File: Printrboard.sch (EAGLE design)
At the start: 127 parts, among them J1 MICROSD, J3 USB-MICRO-PTH, J4 PCIE, Q1 RFP30N06LE, Q2 RFP30N06LE, Q3 RFP30N06LE, U1 LM2841, U10 MCP4728, U2 A4982, U3 A4982, U4 A4982, U5 A4982, U6 AT90USB1286, U7 AP7313, U8 TXB0104, U9 PRTR5V0U4D, X1 16MHz

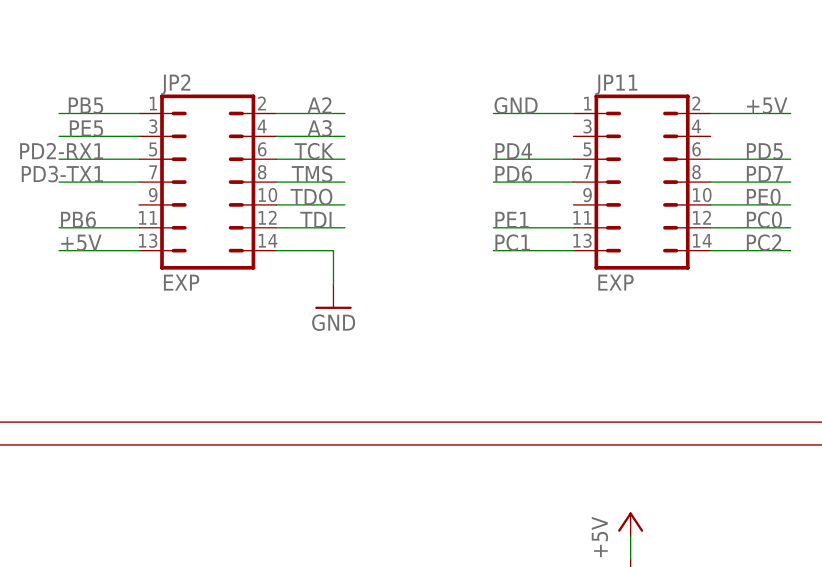
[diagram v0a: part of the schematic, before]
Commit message: Manufacturability changes
Added some pin 1 indicators
Added test point for VBUS signal
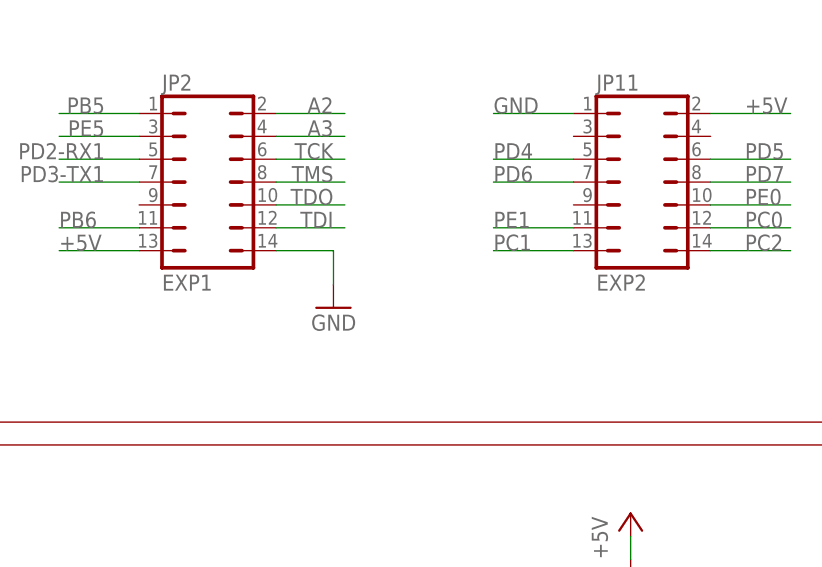
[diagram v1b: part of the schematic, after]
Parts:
- JP11: value EXP -> EXP2
- JP2: value EXP -> EXP1
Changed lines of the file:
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@@
 <part name="JP8" library="SparkFun" deviceset="M03" device="POLAR" value="Y-STOP"/>
 <part name="JP10" library="SparkFun" deviceset="M03" device="POLAR" value="Z-STOP"/>
-<part name="JP2" library="printrbot" deviceset="JP7Q" device="" value="EXP"/>
-<part name="JP11" library="printrbot" deviceset="JP7Q" device="" value="EXP"/>
+<part name="JP2" library="printrbot" deviceset="JP7Q" device="" value="EXP1"/>
+<part name="JP11" library="printrbot" deviceset="JP7Q" device="" value="EXP2"/>
 <part name="JP4" library="printrbot" deviceset="JP3Q" device="" value="ICSP"/>
 <part name="C34" library="ipc-7351-capacitor" deviceset="CAPACITOR_" device="0805" value="0.1uF"/>

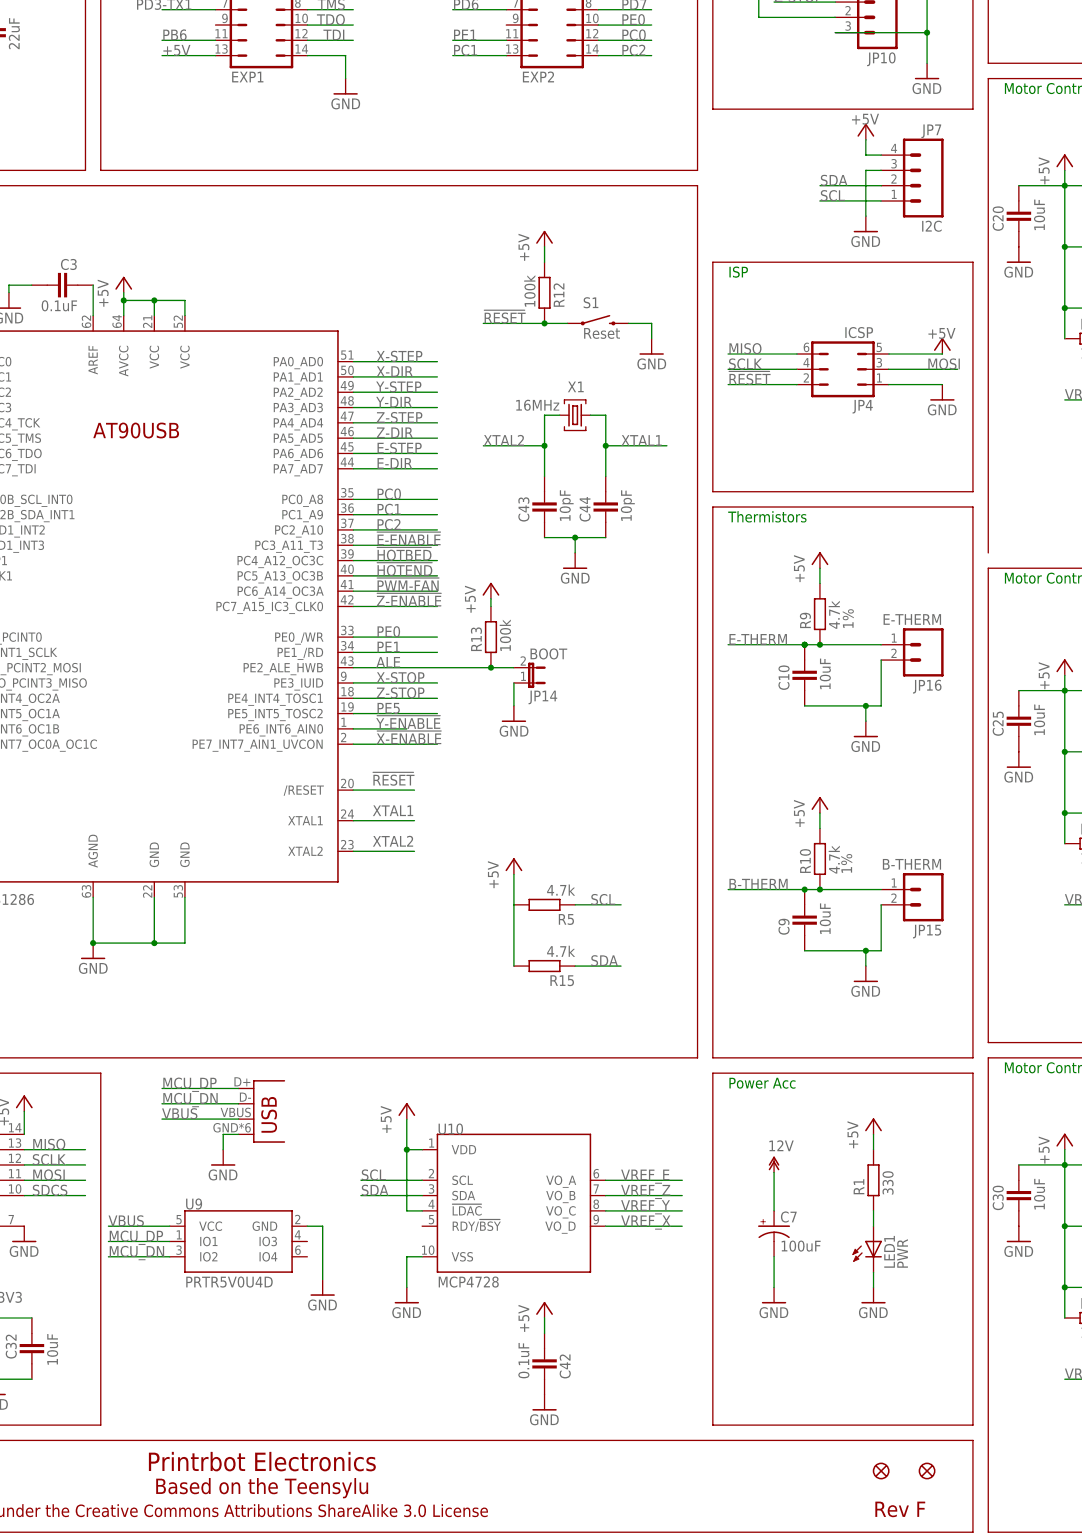
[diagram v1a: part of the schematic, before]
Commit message: Minor schematic changes
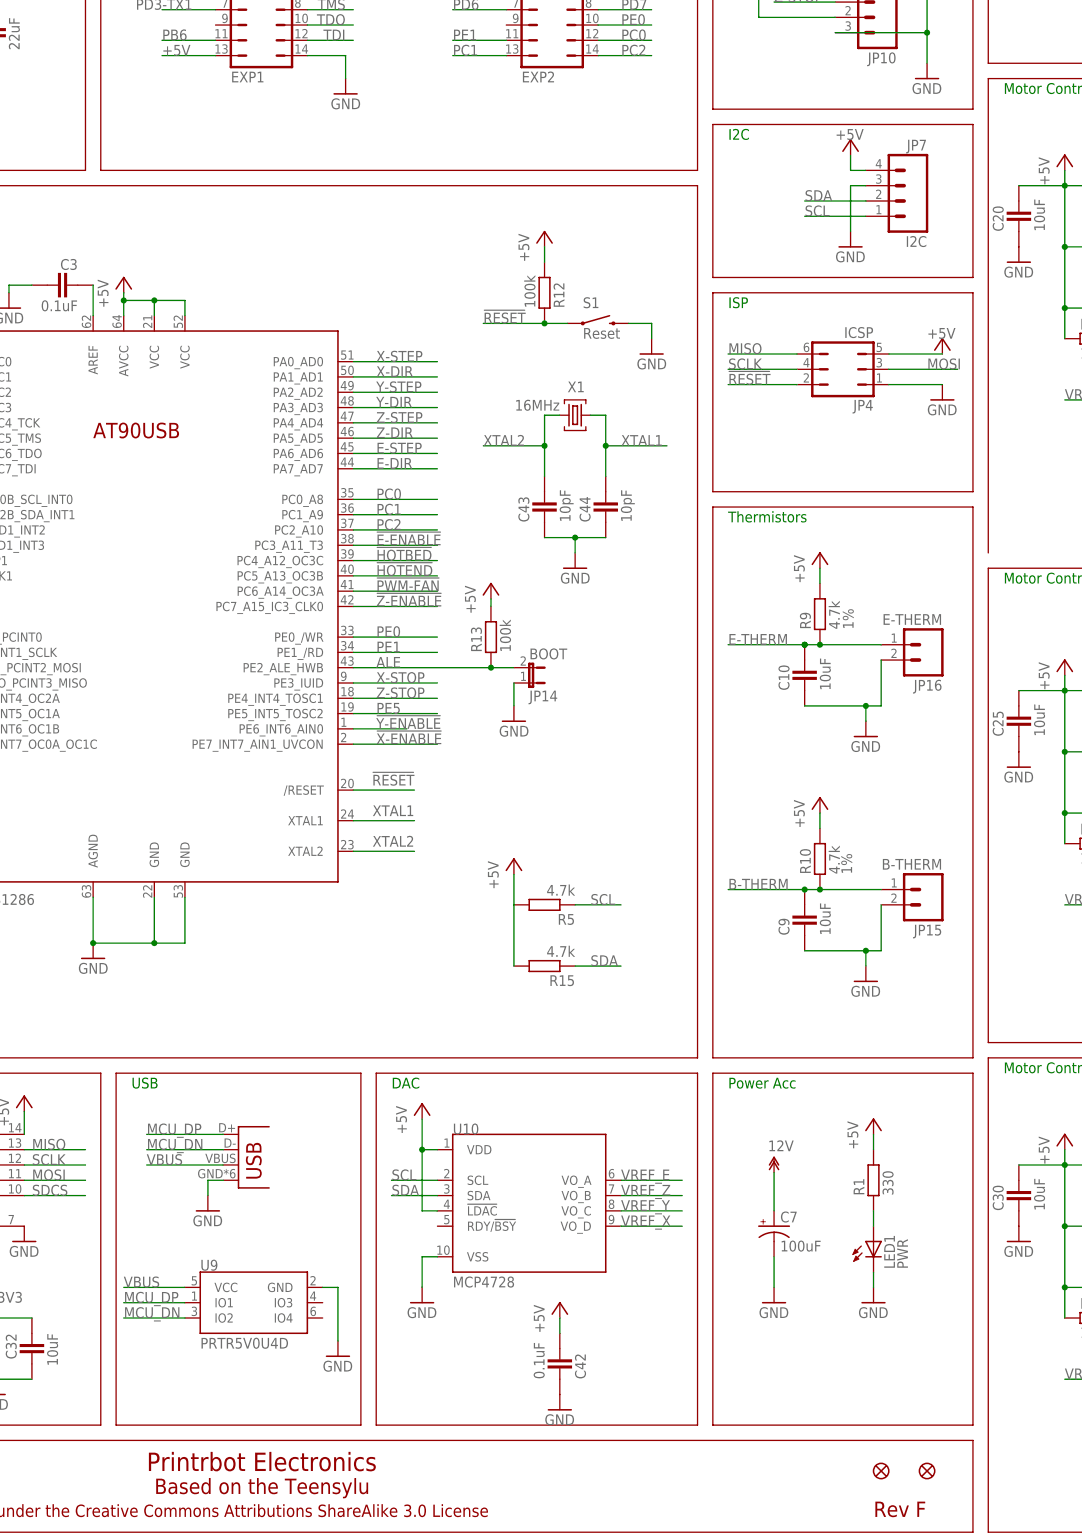
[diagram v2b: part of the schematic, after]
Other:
- note added: "DAC"
- note added: "I2C"
- note added: "USB"
- moved on the sheet: C42, JP7, U10, U9

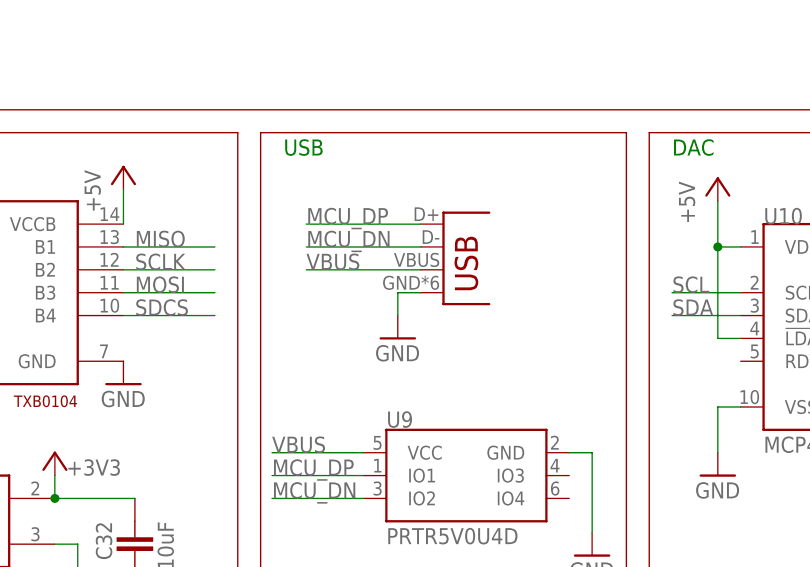
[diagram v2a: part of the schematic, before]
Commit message: Redraw USB connector for manufacturability
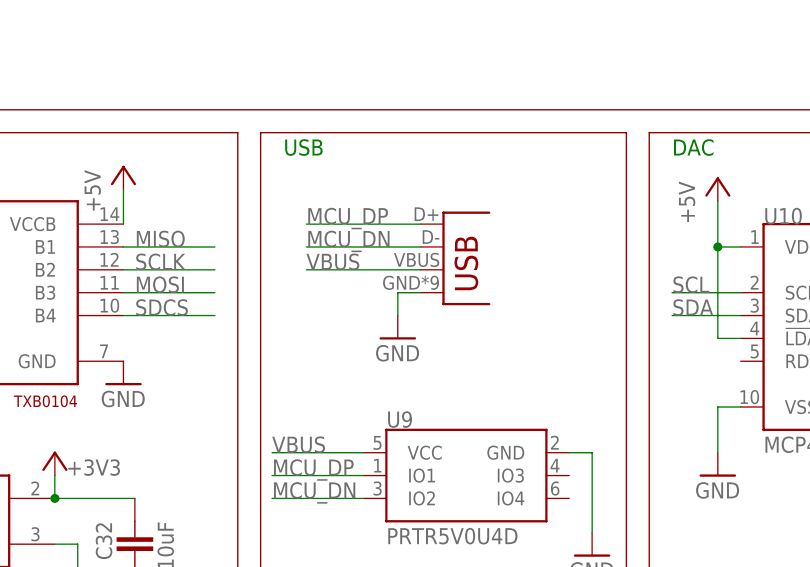
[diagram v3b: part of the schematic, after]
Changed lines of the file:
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@@
 <?xml version="1.0" encoding="utf-8"?>
 <!DOCTYPE eagle SYSTEM "eagle.dtd">
-<eagle version="6.1">
+<eagle version="6.6.0">
 <drawing>
 <settings>

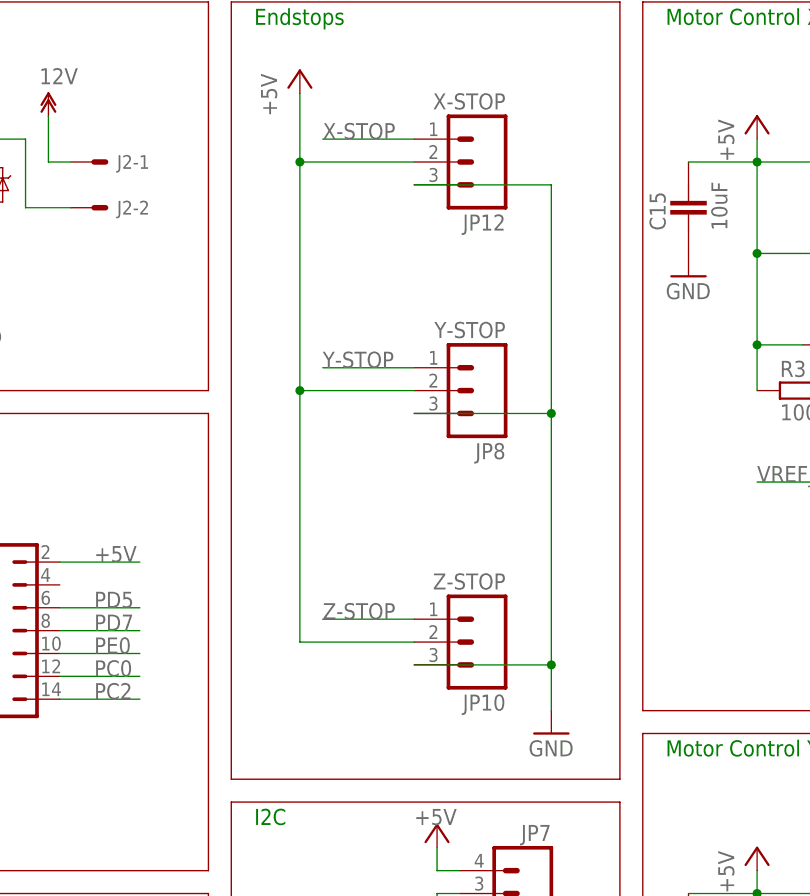
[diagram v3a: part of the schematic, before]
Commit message: Add in voltage selection and input buffering for the Z-stop
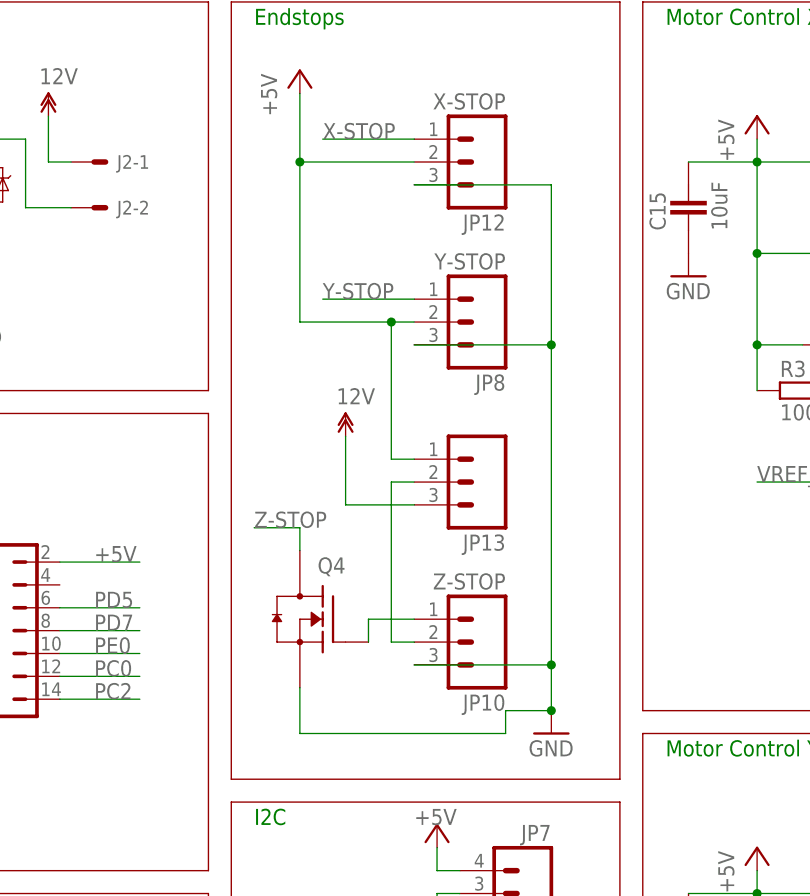
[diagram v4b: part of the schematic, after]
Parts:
- added JP13: (no value), SparkFun:M03PTH
- added Q4: RFP30N06LE, ipc-7351-transistor:MOSFET-NCH_SOT-23
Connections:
- new net N$6: JP10.1, Q4.G
- new net N$8: JP10.2, JP13.2
- net +5V: now also JP13.1; no longer JP10.2
- net 12V: now also JP13.3
- net GND: now also Q4.S
- net Z-STOP: now also Q4.D; no longer JP10.1
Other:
- moved on the sheet: JP8
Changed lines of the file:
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@@
 <part name="GND52" library="SparkFun" deviceset="GND" device=""/>
 <part name="D2" library="printrbot" deviceset="SCH-DIODE" device="SMA" value=""/>
+<part name="Q4" library="ipc-7351-transistor" deviceset="MOSFET-NCH_" device="SOT-23" value="RFP30N06LE"/>
+<part name="U$6" library="12v" deviceset="12V" device=""/>
+<part name="JP13" library="SparkFun" deviceset="M03" device="PTH"/>
 </parts>
 <sheets>
@@
 </instance>
 <instance part="JP6" gate="G$1" x="127" y="220.98" rot="MR0"/>
-<instance part="JP8" gate="G$1" x="223.52" y="198.12" rot="R180"/>
+<instance part="JP8" gate="G$1" x="223.52" y="205.74" rot="R180"/>
 <instance part="JP10" gate="G$1" x="223.52" y="170.18" rot="R180"/>
 <instance part="JP2" gate="B" x="120.65" y="171.45" rot="R270"/>
@@
 <instance part="GND52" gate="1" x="172.72" y="78.74" rot="MR0"/>
 <instance part="D2" gate="G$1" x="60.96" y="215.9" rot="R90"/>
+<instance part="Q4" gate="G$1" x="208.28" y="172.72" smashed="yes" rot="MR0">
+<attribute name="NAME" x="208.28" y="177.8" size="1.778" layer="95" rot="MR0"/>
+</instance>
+<instance part="U$6" gate="G$1" x="208.28" y="193.04"/>
+<instance part="JP13" gate="G$1" x="223.52" y="187.96" rot="R180"/>
 </instances>
 <busses>
@@
 <segment>
 <wire x1="215.9" y1="220.98" x2="231.14" y2="220.98" width="0.1524" layer="91"/>
-<wire x1="231.14" y1="220.98" x2="231.14" y2="195.58" width="0.1524" layer="91"/>
-<wire x1="231.14" y1="195.58" x2="231.14" y2="167.64" width="0.1524" layer="91"/>
+<wire x1="231.14" y1="220.98" x2="231.14" y2="203.2" width="0.1524" layer="91"/>
+<wire x1="231.14" y1="203.2" x2="231.14" y2="167.64" width="0.1524" layer="91"/>
 <wire x1="231.14" y1="167.64" x2="231.14" y2="162.56" width="0.1524" layer="91"/>
-<wire x1="215.9" y1="195.58" x2="231.14" y2="195.58" width="0.1524" layer="91"/>
+<wire x1="215.9" y1="203.2" x2="231.14" y2="203.2" width="0.1524" layer="91"/>
 <wire x1="215.9" y1="167.64" x2="231.14" y2="167.64" width="0.1524" layer="91"/>
-<junction x="231.14" y="195.58"/>
+<junction x="231.14" y="203.2"/>
 <junction x="231.14" y="167.64"/>
 <pinref part="JP12" gate="G$1" pin="3"/>
@@
 <pinref part="JP8" gate="G$1" pin="3"/>
 <pinref part="JP10" gate="G$1" pin="3"/>
+<wire x1="203.2" y1="160.02" x2="226.06" y2="160.02" width="0.1524" layer="91"/>
+<wire x1="226.06" y1="160.02" x2="226.06" y2="162.56" width="0.1524" layer="91"/>
+<wire x1="226.06" y1="162.56" x2="231.14" y2="162.56" width="0.1524" layer="91"/>
+<junction x="231.14" y="162.56"/>
+<pinref part="Q4" gate="G$1" pin="S"/>
+<wire x1="203.2" y1="160.02" x2="203.2" y2="165.1" width="0.1524" layer="91"/>
 </segment>
 <segment>
@@
 <junction x="5.08" y="220.98"/>
 </segment>
+<segment>
+<pinref part="JP13" gate="G$1" pin="3"/>
+<wire x1="215.9" y1="185.42" x2="208.28" y2="185.42" width="0.1524" layer="91"/>
+<wire x1="208.28" y1="185.42" x2="208.28" y2="193.04" width="0.1524" layer="91"/>
+<pinref part="U$6" gate="G$1" pin="12V"/>
+</segment>
 </net>
 <net name="MISO" class="0">
@@
 <net name="Y-STOP" class="0">
 <segment>
-<wire x1="215.9" y1="200.66" x2="205.74" y2="200.66" width="0.1524" layer="91"/>
-<label x="205.74" y="200.66" size="1.778" layer="95"/>
+<wire x1="215.9" y1="208.28" x2="205.74" y2="208.28" width="0.1524" layer="91"/>
+<label x="205.74" y="208.28" size="1.778" layer="95"/>
 <pinref part="JP8" gate="G$1" pin="1"/>
 </segment>
@@
 <net name="Z-STOP" class="0">
 <segment>
-<wire x1="215.9" y1="172.72" x2="205.74" y2="172.72" width="0.1524" layer="91"/>
-<label x="205.74" y="172.72" size="1.778" layer="95"/>
-<pinref part="JP10" gate="G$1" pin="1"/>
-</segment>
-<segment>
 <wire x1="135.89" y1="57.15" x2="149.86" y2="57.15" width="0.1524" layer="91"/>
 <label x="139.7" y="57.15" size="1.778" layer="95"/>
 <pinref part="U6" gate="G$1" pin="PE4_INT4_TOSC1"/>
+</segment>
+<segment>
+<wire x1="203.2" y1="182.88" x2="198.12" y2="182.88" width="0.1524" layer="91"/>
+<label x="198.12" y="182.88" size="1.778" layer="95"/>
+<pinref part="Q4" gate="G$1" pin="D"/>
+<wire x1="203.2" y1="180.34" x2="203.2" y2="182.88" width="0.1524" layer="91"/>
 </segment>
 </net>
@@
 </segment>
 <segment>
-<wire x1="215.9" y1="170.18" x2="203.2" y2="170.18" width="0.1524" layer="91"/>
-<wire x1="215.9" y1="198.12" x2="203.2" y2="198.12" width="0.1524" layer="91"/>
+<wire x1="215.9" y1="205.74" x2="213.36" y2="205.74" width="0.1524" layer="91"/>
+<wire x1="213.36" y1="205.74" x2="203.2" y2="205.74" width="0.1524" layer="91"/>
 <wire x1="215.9" y1="223.52" x2="203.2" y2="223.52" width="0.1524" layer="91"/>
-<wire x1="203.2" y1="223.52" x2="203.2" y2="198.12" width="0.1524" layer="91"/>
-<wire x1="203.2" y1="198.12" x2="203.2" y2="170.18" width="0.1524" layer="91"/>
+<wire x1="203.2" y1="223.52" x2="203.2" y2="205.74" width="0.1524" layer="91"/>
 <wire x1="203.2" y1="231.14" x2="203.2" y2="223.52" width="0.1524" layer="91"/>
-<junction x="203.2" y="198.12"/>
 <junction x="203.2" y="223.52"/>
 <pinref part="JP12" gate="G$1" pin="2"/>
 <pinref part="P+11" gate="1" pin="+5V"/>
 <pinref part="JP8" gate="G$1" pin="2"/>
-<pinref part="JP10" gate="G$1" pin="2"/>
+<pinref part="JP13" gate="G$1" pin="1"/>
+<wire x1="215.9" y1="190.5" x2="213.36" y2="190.5" width="0.1524" layer="91"/>
+<wire x1="213.36" y1="190.5" x2="213.36" y2="205.74" width="0.1524" layer="91"/>
+<junction x="213.36" y="205.74"/>
 </segment>
 <segment>
@@
 </segment>
 </net>
+<net name="N$8" class="0">
+<segment>
+<pinref part="JP10" gate="G$1" pin="2"/>
+<wire x1="215.9" y1="170.18" x2="213.36" y2="170.18" width="0.1524" layer="91"/>
+<wire x1="213.36" y1="170.18" x2="213.36" y2="187.96" width="0.1524" layer="91"/>
+<pinref part="JP13" gate="G$1" pin="2"/>
+<wire x1="215.9" y1="187.96" x2="213.36" y2="187.96" width="0.1524" layer="91"/>
+</segment>
+</net>
+<net name="N$6" class="0">
+<segment>
+<pinref part="JP10" gate="G$1" pin="1"/>
+<wire x1="215.9" y1="172.72" x2="210.82" y2="172.72" width="0.1524" layer="91"/>
+<pinref part="Q4" gate="G$1" pin="G"/>
+<wire x1="210.82" y1="172.72" x2="210.82" y2="170.18" width="0.1524" layer="91"/>
+</segment>
+</net>

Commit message: Bump rev to F5 and update copyright date
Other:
- note added: "Rev F5"
- note removed: "Rev F"
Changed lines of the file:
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@@
 <text x="198.12" y="-7.62" size="1.778" layer="91" font="vector">Power Acc</text>
 <text x="6.35" y="-76.2" size="5.08" layer="94" ratio="10">Printrboard</text>
-<text x="222.25" y="-78.74" size="2.54" layer="94">Rev F</text>
+<text x="222.25" y="-78.74" size="2.54" layer="94">Rev F5</text>
 <text x="101.6" y="-71.12" size="3.048" layer="94">Printrbot Electronics</text>
 <text x="64.77" y="-78.74" size="2.032" layer="94">Licensed under the Creative Commons Attributions ShareAlike 3.0 License</text>
